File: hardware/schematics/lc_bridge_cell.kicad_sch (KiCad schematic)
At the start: 2 parts

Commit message: fix(hardware): restore edge cuts boundary, re-anchor castellated pads, and export production files
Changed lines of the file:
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@@
       (effects (font (size 1.27 1.27)) (hide yes))
+    )
+    (instances
+      (project ""
+        (path "/fbb9c354-eca0-5572-8ad2-3ba0ccc093be/b1000001-0001-4001-b001-000000000001"
+          (reference "B1_#PWR001") (unit 1)
+        )
+        (path "/fbb9c354-eca0-5572-8ad2-3ba0ccc093be/b2000002-0002-4002-b002-000000000002"
+          (reference "B2_#PWR001") (unit 1)
+        )
+        (path "/fbb9c354-eca0-5572-8ad2-3ba0ccc093be/b3000003-0003-4003-b003-000000000003"
+          (reference "B3_#PWR001") (unit 1)
+        )
+        (path "/fbb9c354-eca0-5572-8ad2-3ba0ccc093be/b4000004-0004-4004-b004-000000000004"
+          (reference "B4_#PWR001") (unit 1)
+        )
+        (path "/fbb9c354-eca0-5572-8ad2-3ba0ccc093be/b5000005-0005-4005-b005-000000000005"
+          (reference "B5_#PWR001") (unit 1)
+        )
+        (path "/fbb9c354-eca0-5572-8ad2-3ba0ccc093be/b6000006-0006-4006-b006-000000000006"
+          (reference "B6_#PWR001") (unit 1)
+        )
+        (path "/fbb9c354-eca0-5572-8ad2-3ba0ccc093be/b7000007-0007-4007-b007-000000000007"
+          (reference "B7_#PWR001") (unit 1)
+        )
+        (path "/fbb9c354-eca0-5572-8ad2-3ba0ccc093be/b8000008-0008-4008-b008-000000000008"
+          (reference "B8_#PWR001") (unit 1)
+        )
+        (path "/fbb9c354-eca0-5572-8ad2-3ba0ccc093be/b9000009-0009-4009-b009-000000000009"
+          (reference "B9_#PWR001") (unit 1)
+        )
+        (path "/fbb9c354-eca0-5572-8ad2-3ba0ccc093be/ba000010-0010-4010-b010-000000000010"
+          (reference "B10_#PWR001") (unit 1)
+        )
+        (path "/fbb9c354-eca0-5572-8ad2-3ba0ccc093be/bb000011-0011-4011-b011-000000000011"
+          (reference "B11_#PWR001") (unit 1)
+        )
+        (path "/fbb9c354-eca0-5572-8ad2-3ba0ccc093be/bc000012-0012-4012-b012-000000000012"
+          (reference "B12_#PWR001") (unit 1)
+        )
+        (path "/fbb9c354-eca0-5572-8ad2-3ba0ccc093be/bd000013-0013-4013-b013-000000000013"
+          (reference "B13_#PWR001") (unit 1)
+        )
+        (path "/fbb9c354-eca0-5572-8ad2-3ba0ccc093be/be000014-0014-4014-b014-000000000014"
+          (reference "B14_#PWR001") (unit 1)
+        )
+        (path "/fbb9c354-eca0-5572-8ad2-3ba0ccc093be/bf000015-0015-4015-b015-000000000015"
+          (reference "B15_#PWR001") (unit 1)
+        )
+      )
     )
   )
@@
       (at 300 200 0)
       (effects (font (size 1.27 1.27)))
+    )
+    (instances
+      (project ""
+        (path "/fbb9c354-eca0-5572-8ad2-3ba0ccc093be/b1000001-0001-4001-b001-000000000001"
+          (reference "B1_L1") (unit 1)
+        )
+        (path "/fbb9c354-eca0-5572-8ad2-3ba0ccc093be/b2000002-0002-4002-b002-000000000002"
+          (reference "B2_L1") (unit 1)
+        )
+        (path "/fbb9c354-eca0-5572-8ad2-3ba0ccc093be/b3000003-0003-4003-b003-000000000003"
+          (reference "B3_L1") (unit 1)
+        )
+        (path "/fbb9c354-eca0-5572-8ad2-3ba0ccc093be/b4000004-0004-4004-b004-000000000004"
+          (reference "B4_L1") (unit 1)
+        )
+        (path "/fbb9c354-eca0-5572-8ad2-3ba0ccc093be/b5000005-0005-4005-b005-000000000005"
+          (reference "B5_L1") (unit 1)
+        )
+        (path "/fbb9c354-eca0-5572-8ad2-3ba0ccc093be/b6000006-0006-4006-b006-000000000006"
+          (reference "B6_L1") (unit 1)
+        )
+        (path "/fbb9c354-eca0-5572-8ad2-3ba0ccc093be/b7000007-0007-4007-b007-000000000007"
+          (reference "B7_L1") (unit 1)
+        )
+        (path "/fbb9c354-eca0-5572-8ad2-3ba0ccc093be/b8000008-0008-4008-b008-000000000008"
+          (reference "B8_L1") (unit 1)
+        )
+        (path "/fbb9c354-eca0-5572-8ad2-3ba0ccc093be/b9000009-0009-4009-b009-000000000009"
+          (reference "B9_L1") (unit 1)
+        )
+        (path "/fbb9c354-eca0-5572-8ad2-3ba0ccc093be/ba000010-0010-4010-b010-000000000010"
+          (reference "B10_L1") (unit 1)
+        )
+        (path "/fbb9c354-eca0-5572-8ad2-3ba0ccc093be/bb000011-0011-4011-b011-000000000011"
+          (reference "B11_L1") (unit 1)
+        )
+        (path "/fbb9c354-eca0-5572-8ad2-3ba0ccc093be/bc000012-0012-4012-b012-000000000012"
+          (reference "B12_L1") (unit 1)
+        )
+        (path "/fbb9c354-eca0-5572-8ad2-3ba0ccc093be/bd000013-0013-4013-b013-000000000013"
+          (reference "B13_L1") (unit 1)
+        )
+        (path "/fbb9c354-eca0-5572-8ad2-3ba0ccc093be/be000014-0014-4014-b014-000000000014"
+          (reference "B14_L1") (unit 1)
+        )
+        (path "/fbb9c354-eca0-5572-8ad2-3ba0ccc093be/bf000015-0015-4015-b015-000000000015"
+          (reference "B15_L1") (unit 1)
+        )
+      )
     )
   )
@@
       (effects (font (size 1.27 1.27)))
     )
+    (instances
+      (project ""
+        (path "/fbb9c354-eca0-5572-8ad2-3ba0ccc093be/b1000001-0001-4001-b001-000000000001"
+          (reference "B1_D2") (unit 1)
+        )
+        (path "/fbb9c354-eca0-5572-8ad2-3ba0ccc093be/b2000002-0002-4002-b002-000000000002"
+          (reference "B2_D2") (unit 1)
+        )
+        (path "/fbb9c354-eca0-5572-8ad2-3ba0ccc093be/b3000003-0003-4003-b003-000000000003"
+          (reference "B3_D2") (unit 1)
+        )
+        (path "/fbb9c354-eca0-5572-8ad2-3ba0ccc093be/b4000004-0004-4004-b004-000000000004"
+          (reference "B4_D2") (unit 1)
+        )
+        (path "/fbb9c354-eca0-5572-8ad2-3ba0ccc093be/b5000005-0005-4005-b005-000000000005"
+          (reference "B5_D2") (unit 1)
+        )
+        (path "/fbb9c354-eca0-5572-8ad2-3ba0ccc093be/b6000006-0006-4006-b006-000000000006"
+          (reference "B6_D2") (unit 1)
+        )
+        (path "/fbb9c354-eca0-5572-8ad2-3ba0ccc093be/b7000007-0007-4007-b007-000000000007"
+          (reference "B7_D2") (unit 1)
+        )
+        (path "/fbb9c354-eca0-5572-8ad2-3ba0ccc093be/b8000008-0008-4008-b008-000000000008"
+          (reference "B8_D2") (unit 1)
+        )
+        (path "/fbb9c354-eca0-5572-8ad2-3ba0ccc093be/b9000009-0009-4009-b009-000000000009"
+          (reference "B9_D2") (unit 1)
+        )
+        (path "/fbb9c354-eca0-5572-8ad2-3ba0ccc093be/ba000010-0010-4010-b010-000000000010"
+          (reference "B10_D2") (unit 1)
+        )
+        (path "/fbb9c354-eca0-5572-8ad2-3ba0ccc093be/bb000011-0011-4011-b011-000000000011"
+          (reference "B11_D2") (unit 1)
+        )
+        (path "/fbb9c354-eca0-5572-8ad2-3ba0ccc093be/bc000012-0012-4012-b012-000000000012"
+          (reference "B12_D2") (unit 1)
+        )
+        (path "/fbb9c354-eca0-5572-8ad2-3ba0ccc093be/bd000013-0013-4013-b013-000000000013"
+          (reference "B13_D2") (unit 1)
+        )
+        (path "/fbb9c354-eca0-5572-8ad2-3ba0ccc093be/be000014-0014-4014-b014-000000000014"
+          (reference "B14_D2") (unit 1)
+        )
+        (path "/fbb9c354-eca0-5572-8ad2-3ba0ccc093be/bf000015-0015-4015-b015-000000000015"
+          (reference "B15_D2") (unit 1)
+        )
+      )
+    )
   )

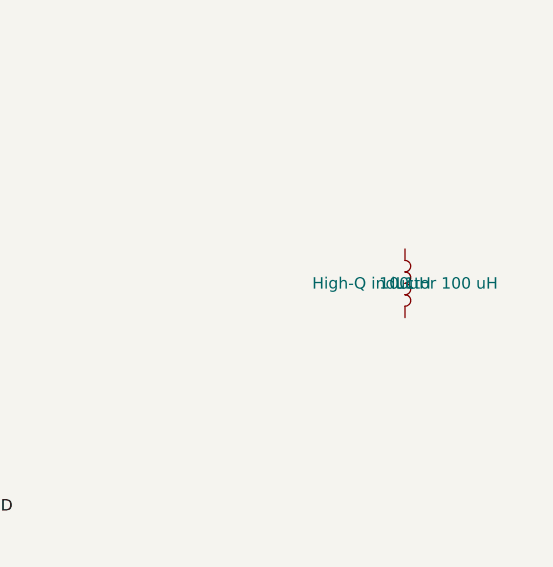
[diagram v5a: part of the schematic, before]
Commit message: fix(hardware): align KiCad schematic inductor values to 100mH matching physical simulation model
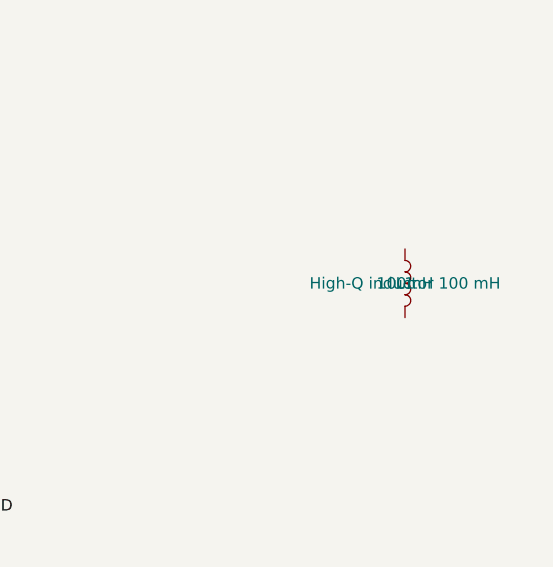
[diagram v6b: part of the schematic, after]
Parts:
- L1: value 100uH -> 100mH
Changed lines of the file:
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@@
       (effects (font (size 1.27 1.27)))
     )
-    (property "Value" "100uH"
+    (property "Value" "100mH"
       (at 300 200 0)
       (effects (font (size 1.27 1.27)))
@@
       (effects (font (size 1.27 1.27)) (hide yes))
     )
-    (property "ki_description" "High-Q inductor 100 uH"
+    (property "ki_description" "High-Q inductor 100 mH"
       (at 300 200 0)
       (effects (font (size 1.27 1.27)))

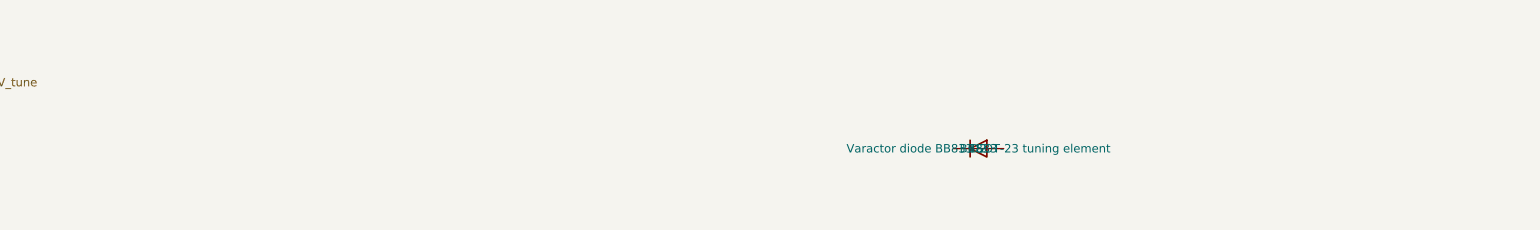
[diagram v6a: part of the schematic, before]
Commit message: docs(hardware): clarify physical analog adaptation circuit mapping for AdEx w state variable
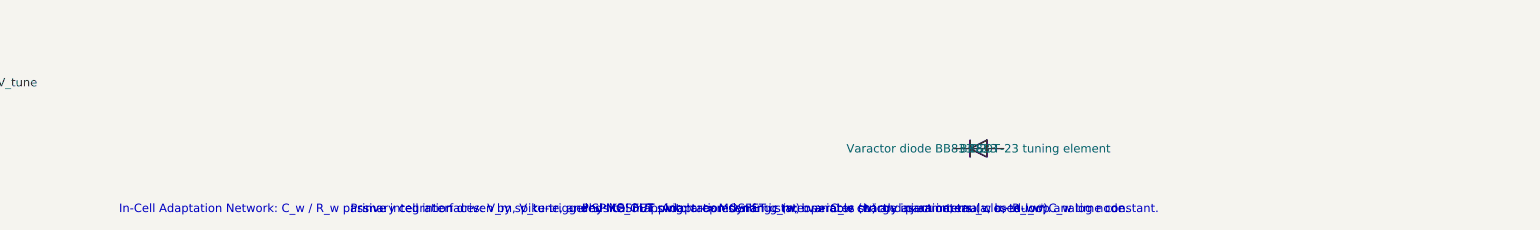
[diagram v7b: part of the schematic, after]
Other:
- note added: "In-Cell Adaptation Network: C_w / R_w passive integration driven by spike-triggered MOSFET switch representing state variable (w) and parameters (a, b, tau_w)."
- note added: "Physical mapping: a -> MOSFET g_m; b -> C_w charge injection; tau_w -> R_w * C_w time constant."
- note added: "Primary cell interfaces: V_m, V_tune, and SPIKE_OUT. Adaptation dynamic (w) operates strictly as an internal closed-loop analog node."
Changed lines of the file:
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@@
     )
   )
+  (text "In-Cell Adaptation Network: C_w / R_w passive integration driven by spike-triggered MOSFET switch representing state variable (w) and parameters (a, b, tau_w)."
+    (exclude_from_sim no)
+    (at 70 260 0)
+    (effects (font (size 1.27 1.27)) (justify left bottom))
 )
+  (text "Primary cell interfaces: V_m, V_tune, and SPIKE_OUT. Adaptation dynamic (w) operates strictly as an internal closed-loop analog node."
+    (exclude_from_sim no)
+    (at 105 260 0)
+    (effects (font (size 1.27 1.27)) (justify left bottom))
+)
+  (text "Physical mapping: a -> MOSFET g_m; b -> C_w charge injection; tau_w -> R_w * C_w time constant."
+    (exclude_from_sim no)
+    (at 140 260 0)
+    (effects (font (size 1.27 1.27)) (justify left bottom))
+)
+)
